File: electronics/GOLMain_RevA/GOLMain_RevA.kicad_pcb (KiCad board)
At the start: 2 copper layers, 18 parts, among them P1 CONN_01X02, P2 CONN_01X02, P3 CONN_01X04, P4 CONN_01X02, U1 LM1117-3.3, U2 ESP8266-12E, U3 74LS165

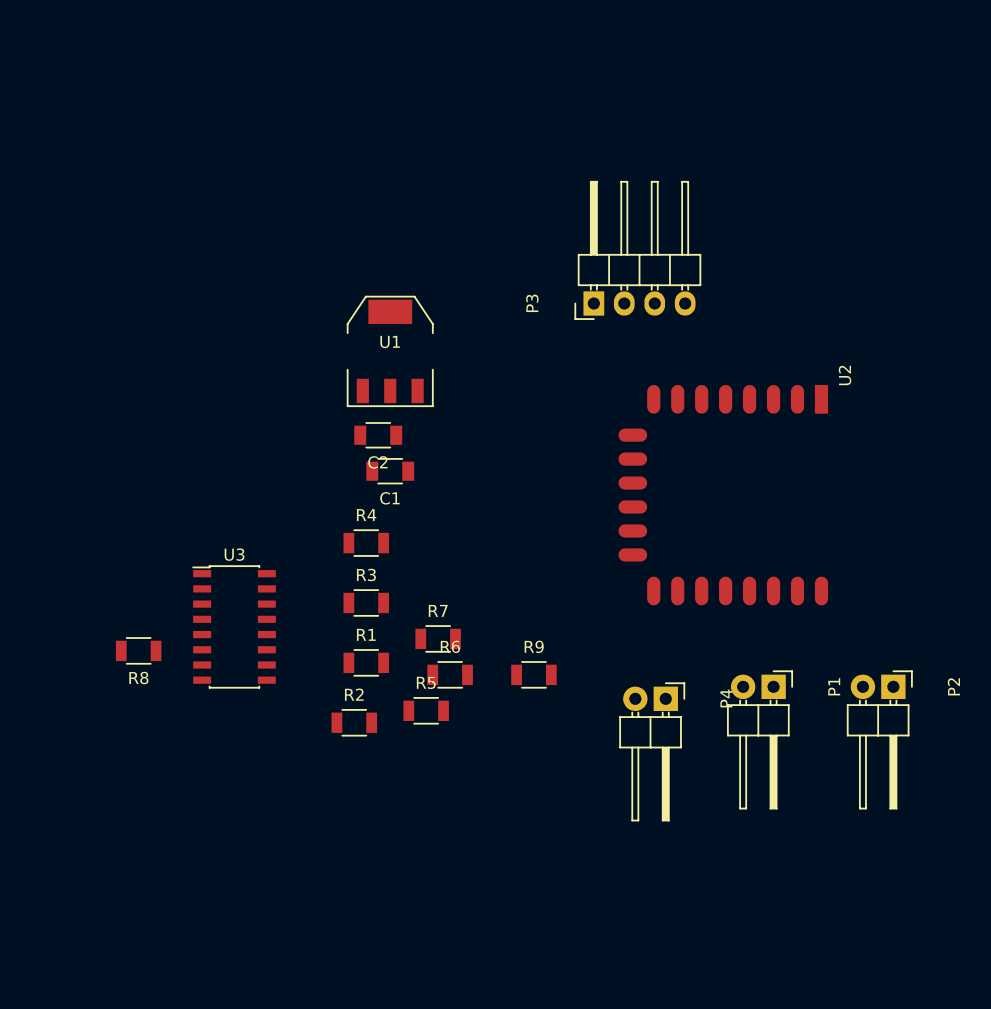
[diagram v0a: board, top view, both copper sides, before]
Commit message: added initial bill of materials mostly consisting of the electronics and power systems with estimated parts list
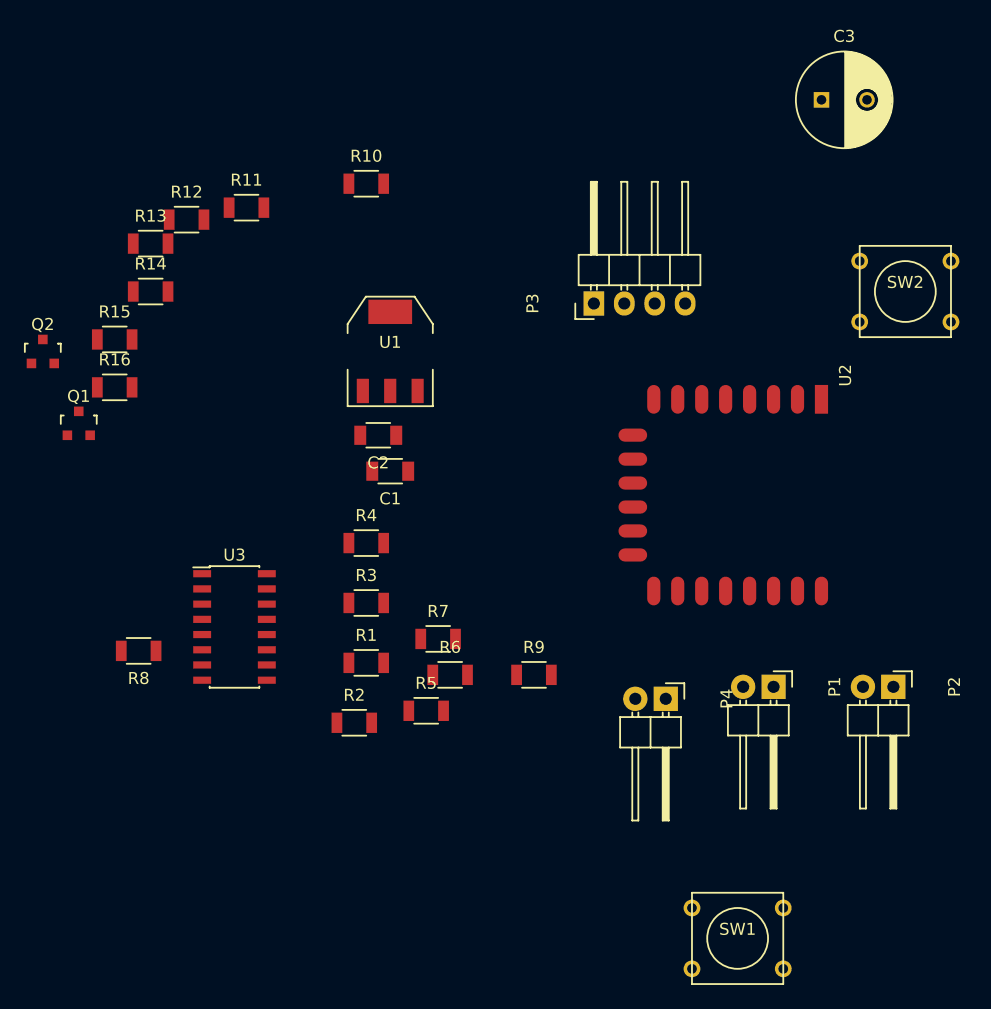
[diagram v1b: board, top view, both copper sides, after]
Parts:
- added C3: 1F, Capacitors_ThroughHole:C_Radial_D8_L13_P3.8, F.Cu at (173.0, 63.0)
- added Q1: BSS138, TO_SOT_Packages_SMD:SOT-23, F.Cu at (111.0, 90.0)
- added Q2: BSS138, TO_SOT_Packages_SMD:SOT-23, F.Cu at (108.0, 84.0)
- added R10: 10K, Resistors_SMD:R_1206, F.Cu at (135.0, 70.0)
- added R11: 10K, Resistors_SMD:R_1206, F.Cu at (125.0, 72.0)
- added R12: 10K, Resistors_SMD:R_1206, F.Cu at (120.0, 73.0)
- added R13: 10K, Resistors_SMD:R_1206, F.Cu at (117.0, 75.0)
- added R14: 10K, Resistors_SMD:R_1206, F.Cu at (117.0, 79.0)
- added R15: 10K, Resistors_SMD:R_1206, F.Cu at (114.0, 83.0)
- added R16: 10K, Resistors_SMD:R_1206, F.Cu at (114.0, 87.0)
- added SW1: SW_PUSH, Buttons_Switches_ThroughHole:SW_PUSH_SMALL, F.Cu at (166.0, 133.0)
- added SW2: SW_PUSH, Buttons_Switches_ThroughHole:SW_PUSH_SMALL, F.Cu at (180.0, 79.0)
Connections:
- R1 pad 2: ID_0 -> (no net)
- R2 pad 2: ID_1 -> (no net)
- R3 pad 2: ID_2 -> (no net)
- R4 pad 2: ID_3 -> (no net)
- R5 pad 2: ID_4 -> (no net)
- R6 pad 2: ID_5 -> (no net)
- R7 pad 2: ID_6 -> (no net)
- R8 pad 2: ID_7 -> (no net)
- U2 pad 10: ID_DATA -> (no net)
- U2 pad 11: Net-(U2-Pad11) -> (no net)
- U2 pad 12: Net-(U2-Pad12) -> (no net)
- U2 pad 13: ID_LATCH -> (no net)
- U2 pad 14: ID_CLOCK -> (no net)
- U2 pad 17: Net-(U2-Pad17) -> READER1
- U2 pad 19: LED_CLOCK -> SDA
- U2 pad 2: Net-(U2-Pad2) -> (no net)
- U2 pad 20: LED_DATA -> SCL
- U2 pad 4: Net-(U2-Pad4) -> READER2
- U2 pad 5: Net-(U2-Pad5) -> ID_CLOCK
- U2 pad 6: READER1 -> ID_DATA
- U2 pad 7: READER2 -> ID_LATCH
- U2 pad 9: Net-(U2-Pad9) -> (no net)
- U3 pad 16: Net-(U3-Pad16) -> V33
- U3 pad 7: Net-(U3-Pad7) -> (no net)
- U3 pad 8: Net-(U3-Pad8) -> GND
- U3 pad 9: Net-(U3-Pad9) -> (no net)

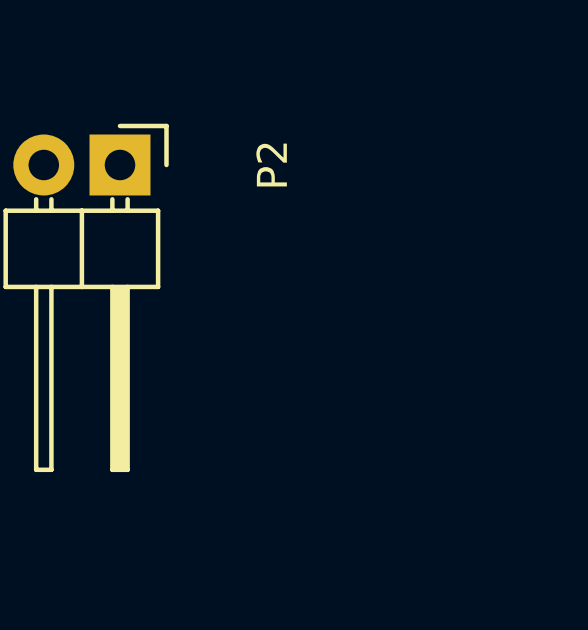
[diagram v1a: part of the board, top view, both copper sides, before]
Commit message: updated schematic and layout for proposed RevA
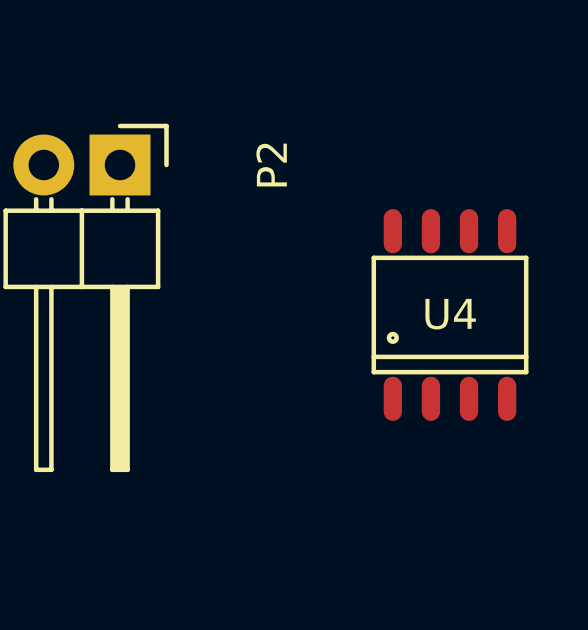
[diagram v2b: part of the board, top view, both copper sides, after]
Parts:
- added U4: SP3485CN, Power_Integrations:SO-8, F.Cu at (190.0, 117.0)
- P1: value CONN_01X02 -> CONN_LEDS
- P2: value CONN_01X02 -> CONN_SERIAL
- P3: value CONN_01X04 -> CONN_READERS
- P4: value CONN_01X02 -> CONN_POWER
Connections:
- R1 pad 2: (no net) -> ID_0
- R2 pad 2: (no net) -> ID_1
- R3 pad 2: (no net) -> ID_2
- R4 pad 2: (no net) -> ID_3
- R5 pad 2: (no net) -> ID_4
- R6 pad 2: (no net) -> ID_5
- R7 pad 2: (no net) -> ID_6
- R8 pad 2: (no net) -> ID_7
- U2 pad 10: (no net) -> Net-(U2-Pad10)
- U2 pad 11: (no net) -> Net-(U2-Pad11)
- U2 pad 12: (no net) -> Net-(U2-Pad12)
- U2 pad 13: (no net) -> Net-(U2-Pad13)
- U2 pad 14: (no net) -> Net-(U2-Pad14)
- U2 pad 2: (no net) -> Net-(U2-Pad2)
- U2 pad 9: (no net) -> Net-(U2-Pad9)
- U3 pad 7: (no net) -> Net-(U3-Pad7)
- U3 pad 9: (no net) -> Net-(U3-Pad9)

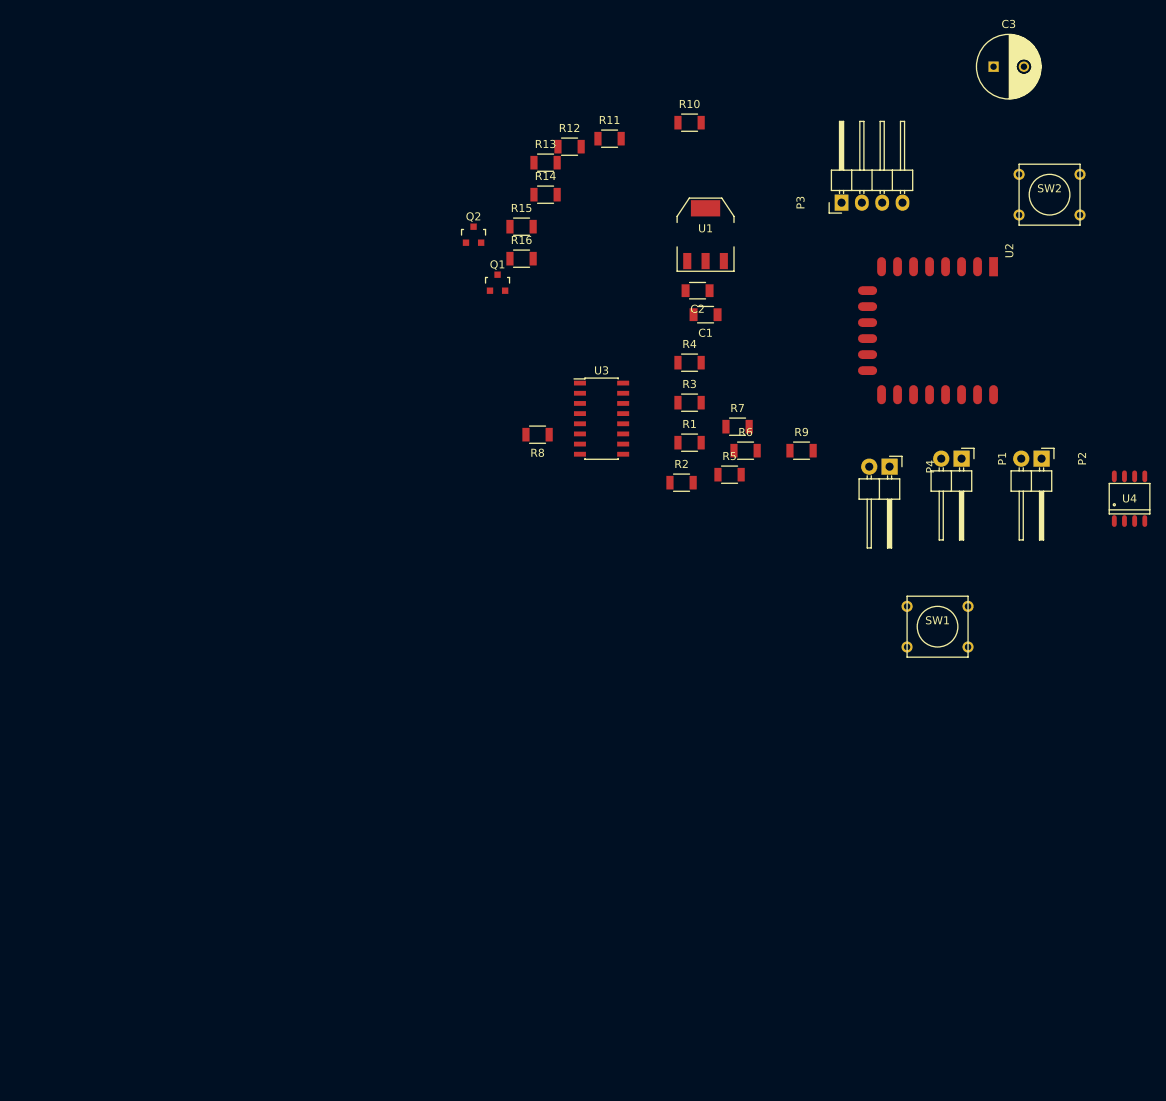
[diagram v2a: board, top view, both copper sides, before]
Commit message: updated main board schematic and layout
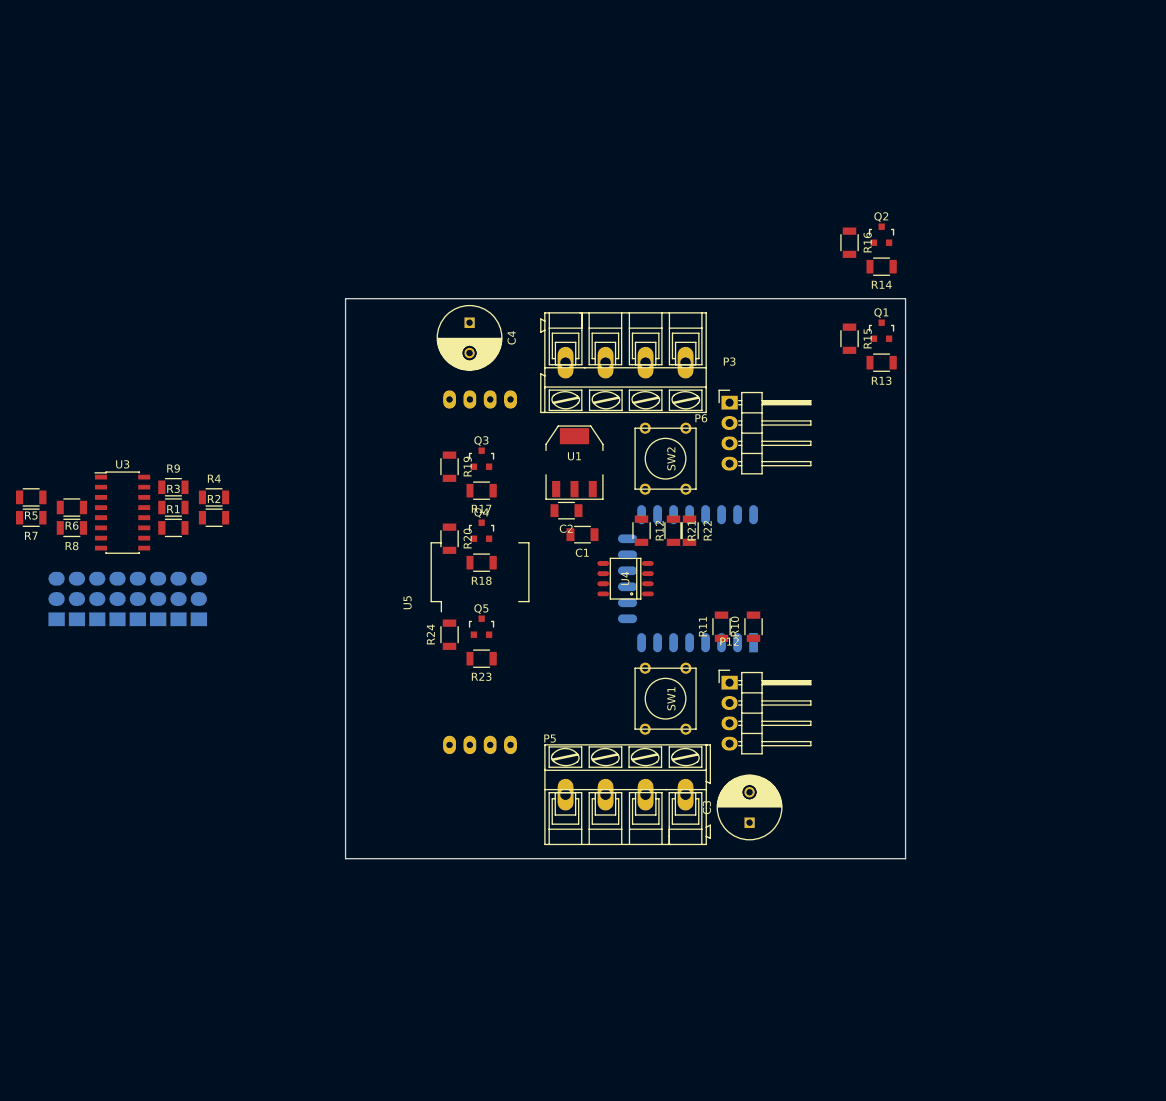
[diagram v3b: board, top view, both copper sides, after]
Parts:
- added C4: 100uF 50V, Capacitors_ThroughHole:C_Radial_D8_L13_P3.8, F.Cu at (107.5, 95.0)
- added P10: CONN_ID_6, Pin_Headers:Pin_Header_Straight_1x03, B.Cu at (71.1, 132.1)
- added P11: CONN_ID_7, Pin_Headers:Pin_Header_Straight_1x03, B.Cu at (73.7, 132.1)
- added P12: CONN_LED, Pin_Headers:Pin_Header_Angled_1x04, F.Cu at (140.0, 140.0)
- added P5: CONN_MAIN1, Connect:AK300-4, F.Cu at (119.5, 154.0)
- added P6: CONN_MAIN2, Connect:AK300-4, F.Cu at (134.5, 100.0)
- added P7: CONN_ID_3, Pin_Headers:Pin_Header_Straight_1x03, B.Cu at (63.5, 132.1)
- added P8: CONN_ID_4, Pin_Headers:Pin_Header_Straight_1x03, B.Cu at (66.0, 132.1)
- added P9: CONN_ID_5, Pin_Headers:Pin_Header_Straight_1x03, B.Cu at (68.6, 132.1)
- added Q3: BSS138, TO_SOT_Packages_SMD:SOT-23, F.Cu at (109.0, 112.0)
- added Q4: BSS138, TO_SOT_Packages_SMD:SOT-23, F.Cu at (109.0, 121.0)
- added Q5: BSS138, TO_SOT_Packages_SMD:SOT-23, F.Cu at (109.0, 133.0)
- added R17: 10K, Resistors_SMD:R_1206, F.Cu at (109.0, 116.0)
- added R18: 10K, Resistors_SMD:R_1206, F.Cu at (109.0, 125.0)
- added R19: 10K, Resistors_SMD:R_1206, F.Cu at (105.0, 113.0)
- added R20: 10K, Resistors_SMD:R_1206, F.Cu at (105.0, 122.0)
- added R21: 10K, Resistors_SMD:R_1206, F.Cu at (133.0, 121.0)
- added R22: 10K, Resistors_SMD:R_1206, F.Cu at (135.0, 121.0)
- added R23: 10K, Resistors_SMD:R_1206, F.Cu at (109.0, 137.0)
- added R24: 10K, Resistors_SMD:R_1206, F.Cu at (105.0, 134.0)
- added U5: MAX485Module, Housings_DIP:DIP-8_W7.62mm_LongPads, F.Cu at (105.0, 130.0)
- C3: value 1F -> 100uF 50V
- P1: value CONN_LEDS -> CONN_ID_0; footprint Pin_Headers:Pin_Header_Angled_1x02 -> Pin_Headers:Pin_Header_Straight_1x03; moved to B.Cu
- P2: value CONN_SERIAL -> CONN_ID_1; footprint Pin_Headers:Pin_Header_Angled_1x02 -> Pin_Headers:Pin_Header_Straight_1x03; moved to B.Cu
- P4: value CONN_POWER -> CONN_ID_2; footprint Pin_Headers:Pin_Header_Angled_1x02 -> Pin_Headers:Pin_Header_Straight_1x03; moved to B.Cu
- SW1, SW2: value SW_PUSH -> SW_PROG
- U2: moved to B.Cu
- moved P2 122.2 mm to (58.4, 132.1), turned to 0 degrees
- moved P1 114.9 mm to (55.9, 132.1), turned to 0 degrees
- moved P4 100.9 mm to (61.0, 132.1), turned to 0 degrees
- moved C3 99.3 mm to (142.5, 157.5), turned to 90 degrees
- moved R7 89.0 mm to (52.7, 119.4), turned to 180 degrees
- moved R5 87.3 mm to (52.7, 116.8), turned to 180 degrees
- moved R6 84.5 mm to (57.8, 118.1), turned to 180 degrees
- moved R9 78.6 mm to (70.5, 115.6)
- moved R3 65.8 mm to (70.5, 118.1)
- moved R1 65.4 mm to (70.5, 120.7)
- moved U4 63.8 mm to (127.0, 127.0), turned to 90 degrees
- moved R10 63.5 mm to (143.0, 133.0), turned to 90 degrees
- moved R11 62.6 mm to (139.0, 133.0), turned to 90 degrees
- moved R4 61.8 mm to (75.6, 116.8)
- moved U3 61.0 mm to (64.1, 118.7)
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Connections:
- P1 pad 1: LED_DATA -> GND
- P1 pad 2: LED_CLOCK -> ID_0
- P2 pad 1: TX -> GND
- P2 pad 2: RX -> ID_1
- P4 pad 2: V12 -> ID_2
- R10 pad 1: Net-(R10-Pad1) -> RESET
- R12 pad 2: Net-(R12-Pad2) -> EN_MAX
- SW1 pad 1: Net-(SW1-Pad1) -> RESET
- SW2 pad 1: GND -> GPIO0
- SW2 pad 2: Net-(R10-Pad1) -> GND
- U2 pad 1: Net-(R10-Pad1) -> RESET
- U2 pad 16: Net-(R12-Pad2) -> EN_MAX
- U2 pad 17: READER1 -> GPIO2
- U2 pad 18: Net-(SW1-Pad1) -> GPIO0
- U2 pad 21: RX -> RX33
- U2 pad 22: TX -> TX33
- U2 pad 5: ID_CLOCK -> READER1
- U2 pad 7: ID_LATCH -> EN_MAX33
- U3 pad 1: ID_LATCH -> GPIO0
- U3 pad 2: ID_CLOCK -> GPIO2
- U4 pad 1: Net-(U4-Pad1) -> RX33
- U4 pad 2: Net-(U4-Pad2) -> EN_MAX
- U4 pad 3: Net-(U4-Pad3) -> EN_MAX
- U4 pad 4: Net-(U4-Pad4) -> TX33
- U4 pad 5: Net-(U4-Pad5) -> GND
- U4 pad 6: Net-(U4-Pad6) -> A
- U4 pad 7: Net-(U4-Pad7) -> B
- U4 pad 8: Net-(U4-Pad8) -> V33
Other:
- board outline added: 70 x 70 mm

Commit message: updated schematics and part selection for layout
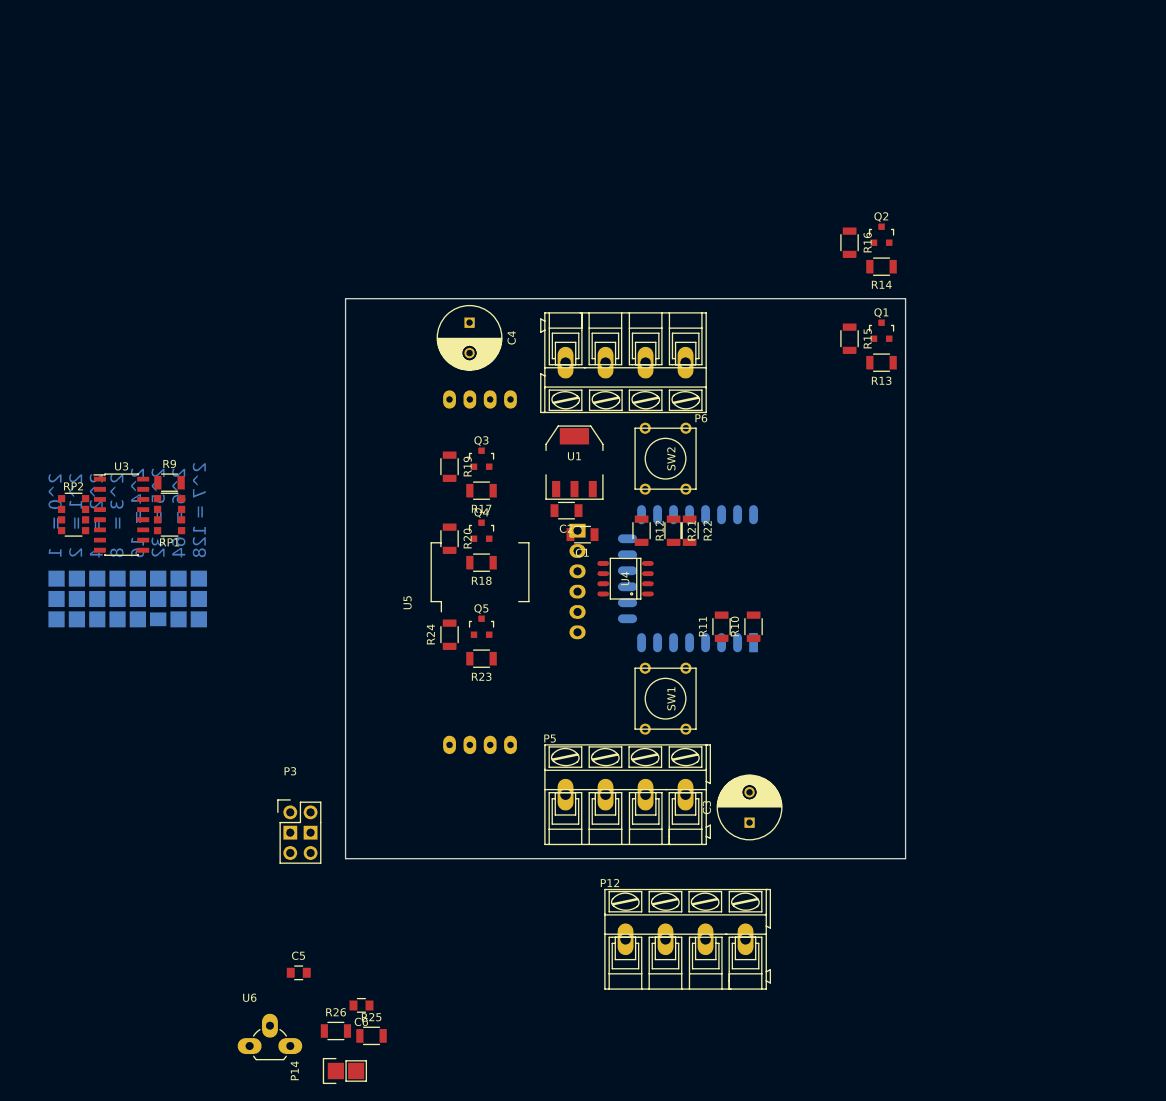
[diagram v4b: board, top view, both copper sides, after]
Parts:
- removed R1, R2, R3, R4, R5, R6, R7, R8: 10K, Resistors_SMD:R_1206
- added C5: 0.1uF, Capacitors_SMD:C_0805, F.Cu at (86.1, 176.3)
- added C6: 0.1uF, Capacitors_SMD:C_0805, F.Cu at (94.0, 180.3)
- added P13: CONN_FTDI, Pin_Headers:Pin_Header_Angled_1x06, B.Cu at (121.0, 121.0)
- added P14: CONN_V50SEL, Pin_Headers:Pin_Header_Straight_1x02, F.Cu at (90.8, 188.5)
- added R25: 56, Resistors_SMD:R_1206, F.Cu at (95.2, 184.2)
- added R26: 39, Resistors_SMD:R_1206, F.Cu at (90.8, 183.5)
- added RP1: R_PACK4_10K, Resistors_SMD:R_Array_Convex_4x1206, F.Cu at (70.0, 119.0)
- added RP2: R_PACK4_10K, Resistors_SMD:R_Array_Convex_4x1206, F.Cu at (58.0, 119.0)
- added U6: LM78L05ACZ, TO_SOT_Packages_THT:TO-92_Rugged, F.Cu at (80.0, 185.4)
- P12: footprint Pin_Headers:Pin_Header_Angled_1x04 -> Connect:AK300-4
- P3: footprint Pin_Headers:Pin_Header_Angled_1x04 -> Pin_Headers:Pin_Header_Straight_2x03
- R13, R14, R15, R16: value 10K -> 1K
- SW1: value SW_PROG -> SW_RESET
- moved P3 75.1 mm to (85.1, 156.2)
- moved P12 34.6 mm to (127.0, 172.1)
- moved R9 0.75 mm to (70.0, 115.0)
- moved U3 0.29 mm to (64.0, 119.0)
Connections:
- P3 pad 1: GND -> V33
- P3 pad 3: READER1 -> GND
- P3 pad 4: READER2 -> GND
- Q4 pad 2: EN_MAX33 -> EN_MAX
- R12 pad 2: EN_MAX -> GPIO15
- R15 pad 2: V12 -> V50
- R16 pad 2: V12 -> V50
- R18 pad 1: EN_MAX33 -> EN_MAX
- U2 pad 16: EN_MAX -> GPIO15
- U2 pad 7: EN_MAX33 -> EN_MAX
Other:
- board text added: "2^0 = 1 2^1 = 2 2^2 = 4 2^3 = 8 2^4 = 16 2^5 = 32 2^6 = 64 2^7 = 128"
